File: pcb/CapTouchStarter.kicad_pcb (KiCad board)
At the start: 4 copper layers, 76.7 x 66.3 mm, 59 parts, among them J1 USB_C_Receptacle, J2 Conn_ARM_JTAG_SWD_10, J3 62684-50110, Q1 SS8050-G, Q2 SS8050-G, SW1 SW_SPDT, SW2 EN, SW3 BOOT, U1 CP2102N-Axx-xQFN28, U2 BD48K33G-TLCT-ND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

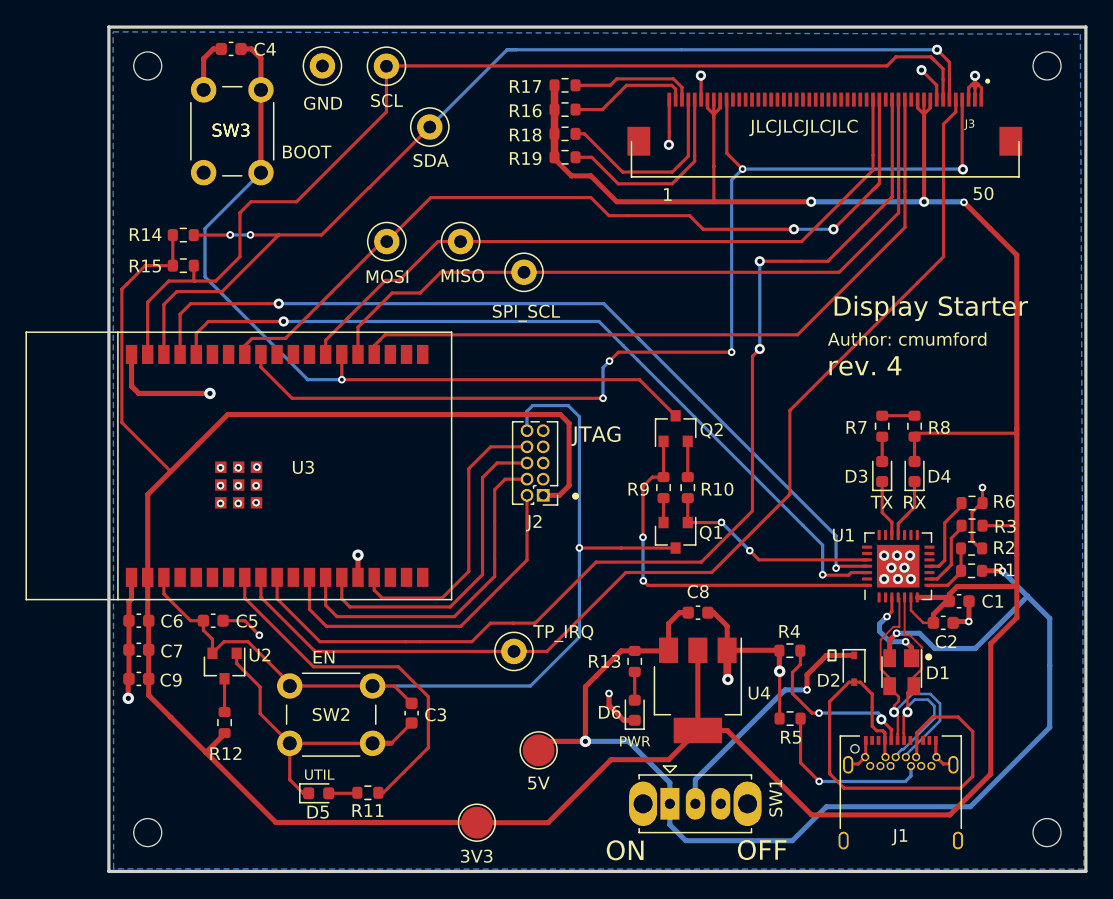
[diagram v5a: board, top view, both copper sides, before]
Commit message: Add JTAG RESET series resistor.
Eliminate the following ERC warning:

    "Pins of type Output and Open collector are connector".

Discussion at
https://www.reddit.com/r/AskElectronics/comments/754epz/series_resistors_on_jtag_lines/

Also, fixed D+/D- ESD pad assignments and a few silkscreen inside
cut boundaries ERC warnings.
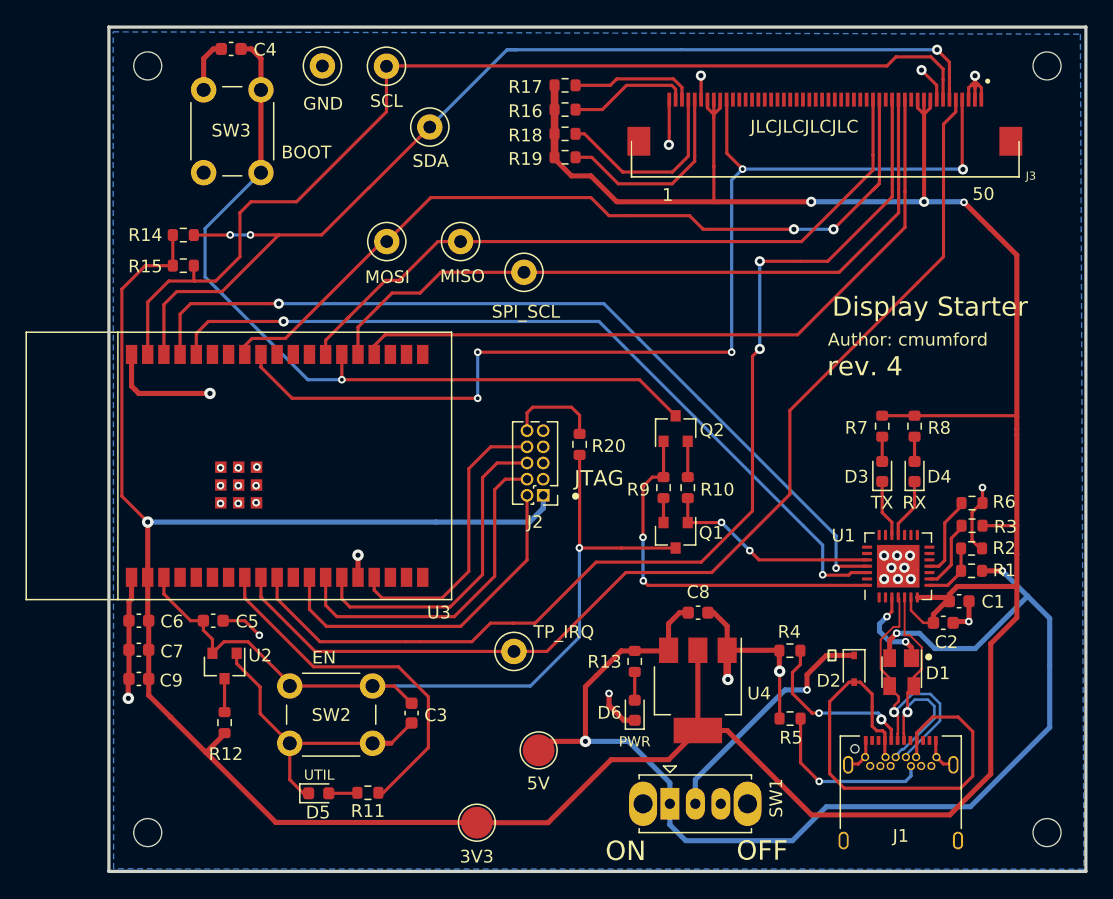
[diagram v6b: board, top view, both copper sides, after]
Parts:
- added R20: 39Ω, Resistor_SMD:R_0603_1608Metric, F.Cu at (165.2, 110.5)
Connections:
- D1 pad 3: D- -> D+
- D1 pad 4: D+ -> D-
- J2 pad 10: EN -> Net-(J2-Pad10)
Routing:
- net +3V3: track 303.8 -> 294.2 mm, vias 3 -> 4
- net EN: track 75.1 -> 66.0 mm
- net Net-(J2-Pad10): track 0.00 -> 7.43 mm
- net RESET: track 85.4 -> 86.1 mm

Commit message: Switch to cmumford-components for KiCad components.
https://github.com/cmumford/cmumford-components.git
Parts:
- J3: footprint 0541325062:0541325062 -> cmumford-footprints:62684-50110
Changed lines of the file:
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@@
       (rotate (xyz 0 0 0))
     )
-    (model "${KIPRJMOD}/library/12401548E412A/1054500101.stp"
+    (model "${KIPRJMOD}/libraries\cmumford-components\3dshapes/1054500101.stp"
       (offset (xyz 0 2 1.5))
       (scale (xyz 1 1 1))
@@
     )
   )
-  (footprint "0541325062:0541325062" (layer "F.Cu")
+  (footprint "cmumford-footprints:62684-50110" (layer "F.Cu")
     (at 185.1152 85.4202 -90)
     (descr "50 Position FFC, FPC Connector Contacts, Bottom 0.020\" (0.50mm) Surface Mount, Right Angle")
@@
     (pad "F1" smd rect locked (at 1.27 -13.97 90) (size 2.27 1.8) (layers "F.Cu" "F.Paste"))
     (pad "F2" smd rect locked (at 1.27 15.24 90) (size 2.27 1.8) (layers "F.Cu" "F.Paste"))
-    (model "${KIPRJMOD}/library/0541325062/footprints.pretty/0541325062.stp"
+    (model "${KIPRJMOD}/libraries/cmumford-components/3dshapes/s62684_501100alf.stp"
       (offset (xyz -1.5 -0.5 0))
       (scale (xyz 1 1 1))
